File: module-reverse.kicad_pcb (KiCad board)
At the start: 2 copper layers, 99 x 90 mm, 20 parts, among them J1 Screw_Terminal_01x04, J2 Screw_Terminal_01x04, J3 Screw_Terminal_01x04, J4 Screw_Terminal_01x04, J5 Screw_Terminal_01x04, K1 AZ733-2CE-12DE, U1 12V

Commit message: Moved power to relay to before the voltage regulator
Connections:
- C1 pad 1: Net-(D1-+) -> /+12V
- C2 pad 1: /+12V -> /+Reg
- C3 pad 1: Net-(D1-+) -> /+12V
- D1 pad 1: Net-(D1-+) -> /+12V
- J2 pad 1: /+12V -> /+Reg
- U1 pad 1: Net-(D1-+) -> /+12V
- U1 pad 3: /+12V -> /+Reg
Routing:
- net /+12V: track 17.9 -> 8.77 mm
- added copper zone on B.Cu, net /+Reg
- removed copper zone on B.Cu, net Net-(D1-+)

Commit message: Added a PTC fuse to the ACC power and an additional LED to show its status
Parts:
- added D4: Green, LED_THT:LED_D3.0mm, F.Cu at (106.2, 76.4)
- added F1: Polyfuse, Fuse:Fuse_BelFuse_0ZRE0005FF_L8.3mm_W3.8mm, F.Cu at (112.2, 91.4)
- added R3: 2.7k, Resistor_THT:R_Axial_DIN0207_L6.3mm_D2.5mm_P10.16mm_Horizontal, F.Cu at (106.2, 69.6)
- U1: value 12V -> MIC2940A-12WT
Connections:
- J4 pad 4: Net-(J2-Pin_3) -> Net-(J4-Pin_4)
- J5 pad 1: Net-(J2-Pin_3) -> Net-(J4-Pin_4)
- R1 pad 2: Net-(J2-Pin_3) -> Net-(J4-Pin_4)
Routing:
- net Net-(J4-Pin_4): track 0.00 -> 132.6 mm
- net Net-(J2-Pin_3): track 170.8 -> 38.6 mm
- net Net-(D4-A): track 0.00 -> 4.26 mm
- net Net-(D2-K): track 161.9 -> 163.1 mm
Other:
- board text added: "Power In"

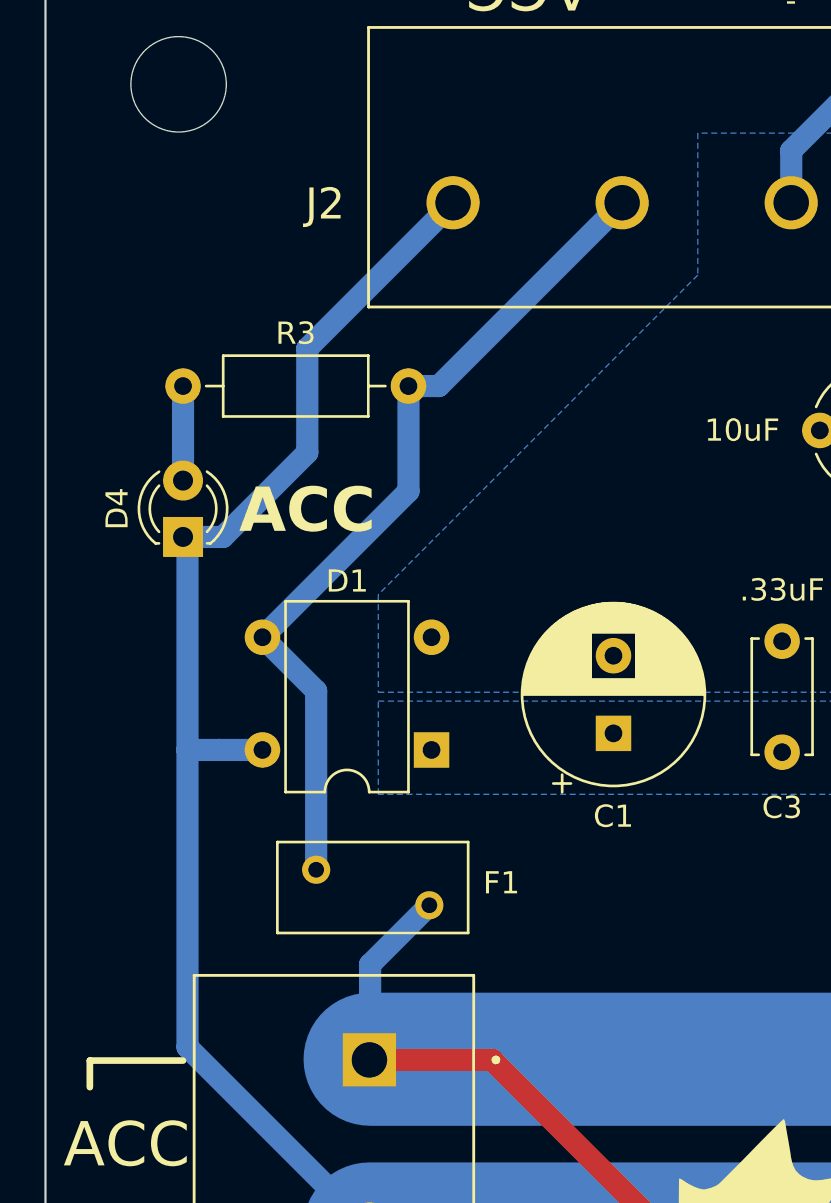
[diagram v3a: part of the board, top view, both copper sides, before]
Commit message: Updated LEDs
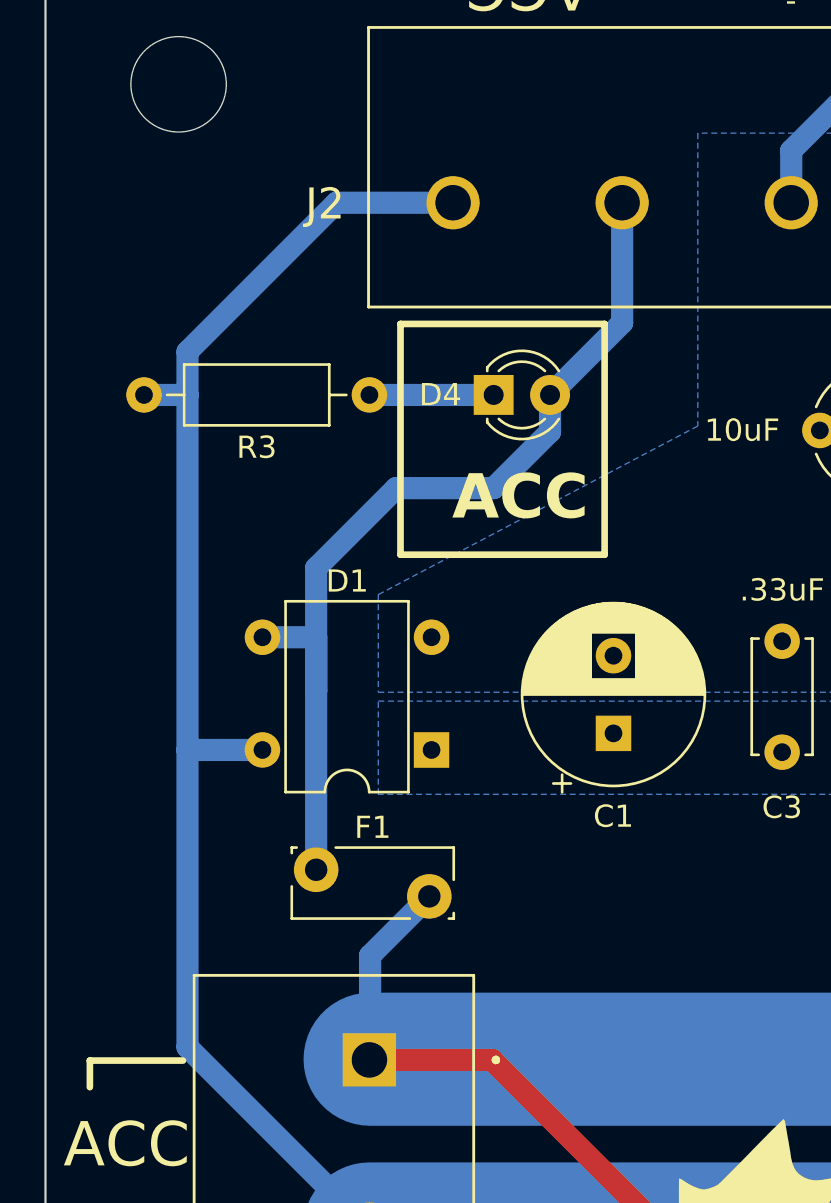
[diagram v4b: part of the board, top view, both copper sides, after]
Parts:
- F1: footprint Fuse:Fuse_BelFuse_0ZRE0005FF_L8.3mm_W3.8mm -> Fuse:Fuse_Bourns_MF-RG300
- moved D4 15.4 mm to (120.2, 70.0), turned to 0 degrees
- moved R3 8.41 mm to (114.6, 70.0), turned to 180 degrees
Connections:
- D1 pad 3: Net-(J2-Pin_3) -> Net-(D4-A)
- D4 pad 1: Net-(D2-K) -> Net-(D4-K)
- F1 pad 1: Net-(J2-Pin_3) -> Net-(D4-A)
- J2 pad 3: Net-(J2-Pin_3) -> Net-(D4-A)
- R3 pad 1: Net-(D4-A) -> Net-(D4-K)
- R3 pad 2: Net-(J2-Pin_3) -> Net-(D2-K)
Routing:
- net Net-(D4-A): track 4.26 -> 43.2 mm
- net Net-(J2-Pin_3): track 38.6 -> 0.00 mm
- net Net-(D4-K): track 0.00 -> 5.60 mm
- net Net-(D2-K): track 163.1 -> 166.9 mm
